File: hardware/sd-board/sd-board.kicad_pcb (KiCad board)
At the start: 2 copper layers, 22 x 71.1 mm, 9 parts, among them J1 TF-01A push-push, J2 FFC 6P 0.5mm, U1 74LVC1G04

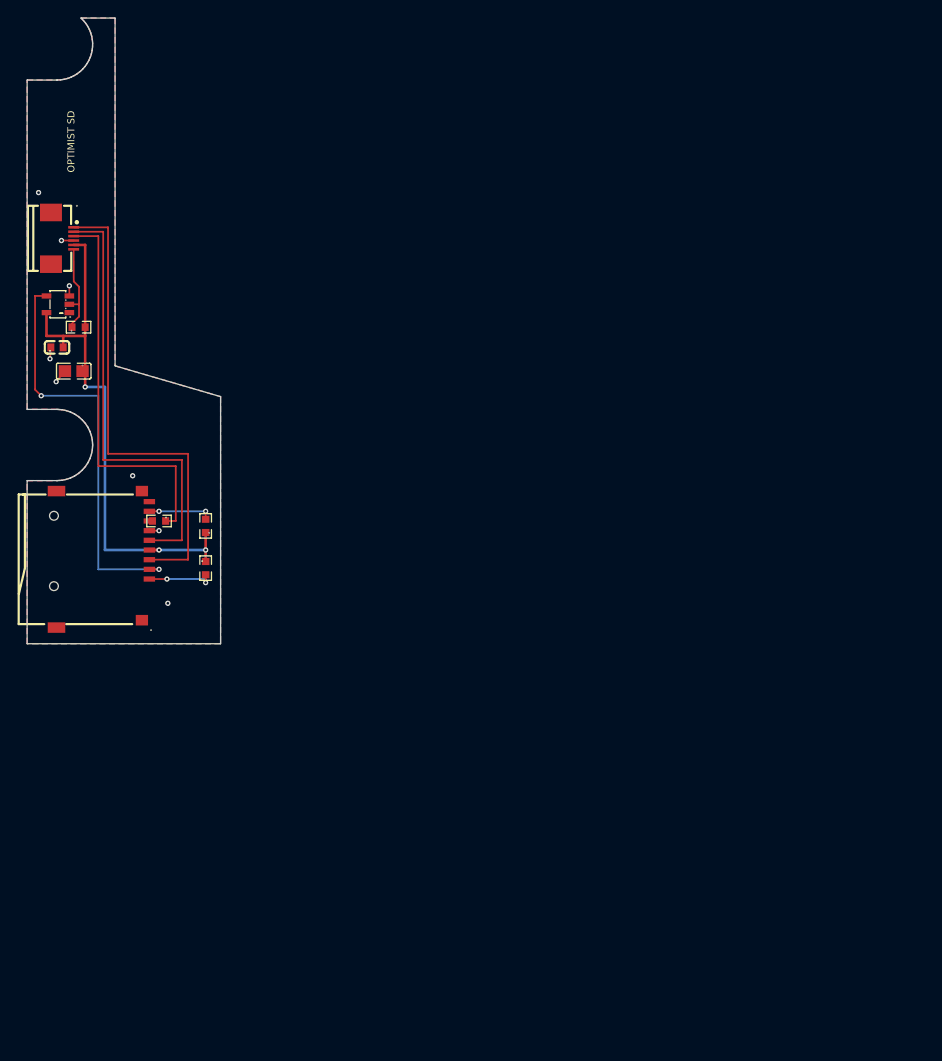
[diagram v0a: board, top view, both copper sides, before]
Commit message: feat(hardware): SD board v4, the user's plan: a 28.8 x 44.5 mm board right of the battery by its plug (the battery stays), the card through the bottom wall flush with the outside at 86 mm from the left wall, the cover's pole in a half-round seat, the FFC from the jacks' gap down to the top; FFC order 3V3 CS MOSI GND CLK MISO (the card's contacts' order, nothing crosses); all sizes measured (MEASUREMENTS.md); DRC 0, nets 0 differ
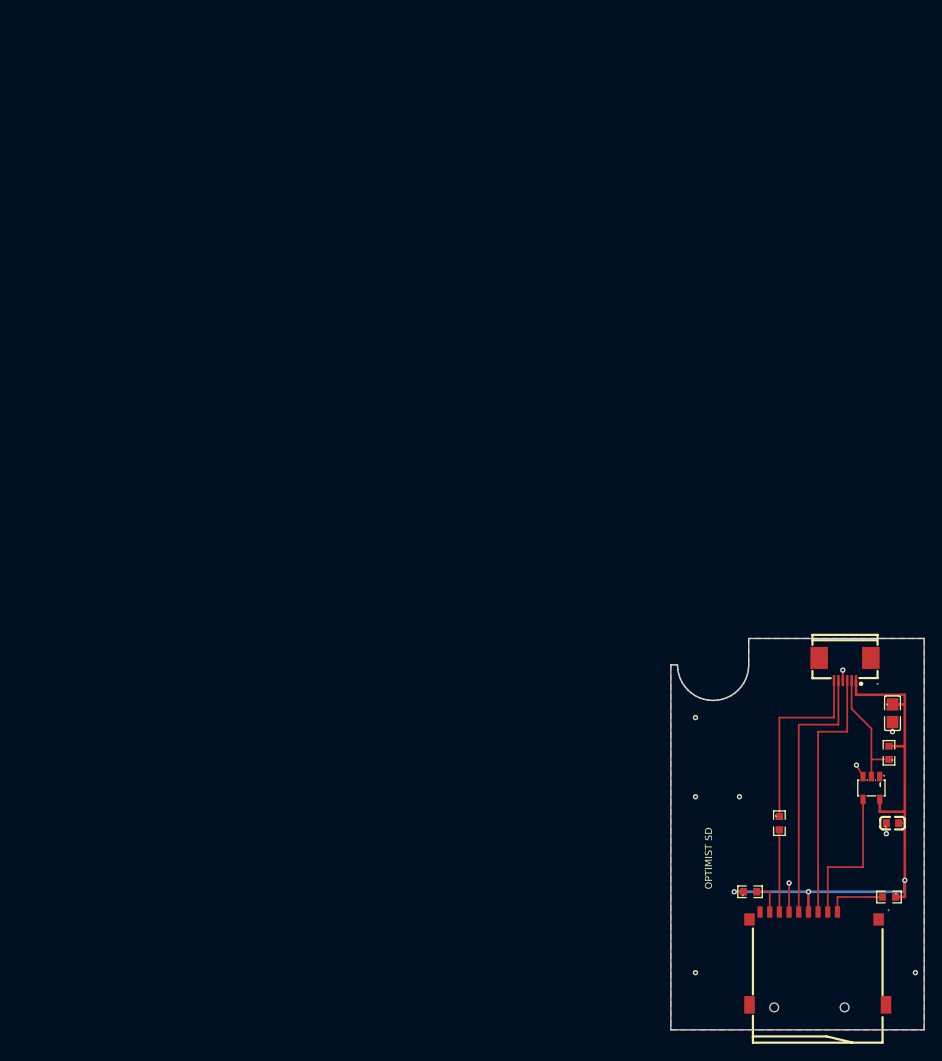
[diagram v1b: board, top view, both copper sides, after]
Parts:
- moved C2 109.3 mm to (198.4, 178.0)
- moved U1 107.6 mm to (196.0, 174.0), turned to 90 degrees
- moved R4 104.1 mm to (198.0, 170.0), turned to 90 degrees
- moved J2 101.6 mm to (193.0, 160.5), turned to 180 degrees
- moved C1 100.9 mm to (198.4, 165.5), turned to -90 degrees
- moved J1 93.1 mm to (189.9, 193.4), turned to 0 degrees
- moved R2 86.2 mm to (198.0, 186.4), turned to 180 degrees
- moved R1 78.5 mm to (185.5, 178.0), turned to -90 degrees
- moved R3 74.6 mm to (182.2, 185.8), turned to 0 degrees
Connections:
- J2 pad 1: MOSI -> 3V3
- J2 pad 2: CLK -> LCD_CS
- J2 pad 3: MISO -> MOSI
- J2 pad 5: 3V3 -> CLK
- J2 pad 6: LCD_CS -> MISO
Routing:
- net CARD_CS: track 47.2 -> 16.8 mm, vias 2 -> 0
- net MOSI: track 55.2 -> 29.6 mm
- net MISO: track 45.1 -> 21.7 mm
- net CLK: track 51.1 -> 30.8 mm
- net DAT0: track 0.35 -> 9.35 mm
- net DAT1: track 7.31 -> 3.79 mm, vias 2 -> 0
- net LCD_CS: track 10.5 -> 13.8 mm
- net GND: track 6.51 -> 8.29 mm, vias 8 -> 10
- net 3V3: track 62.4 -> 63.4 mm
- net DAT2: track 7.71 -> 6.81 mm, vias 2 -> 0
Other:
- board size 22 x 71.1 mm -> 28.8 x 44.5 mm

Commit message: feat(hardware): the SD board's printed tray (make_tray.py, sd-tray.stl, solid): a 0.8 mm floor, grooved rails the board slides into (held up and down; the board narrowed to 26.4 mm for them), a collar round the cover's pole that stops it, posts toward the cover; low elsewhere so the battery's cable crosses over (the user); the board's seat sized for the collar
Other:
- board size 28.8 x 44.5 mm -> 26.4 x 44.5 mm

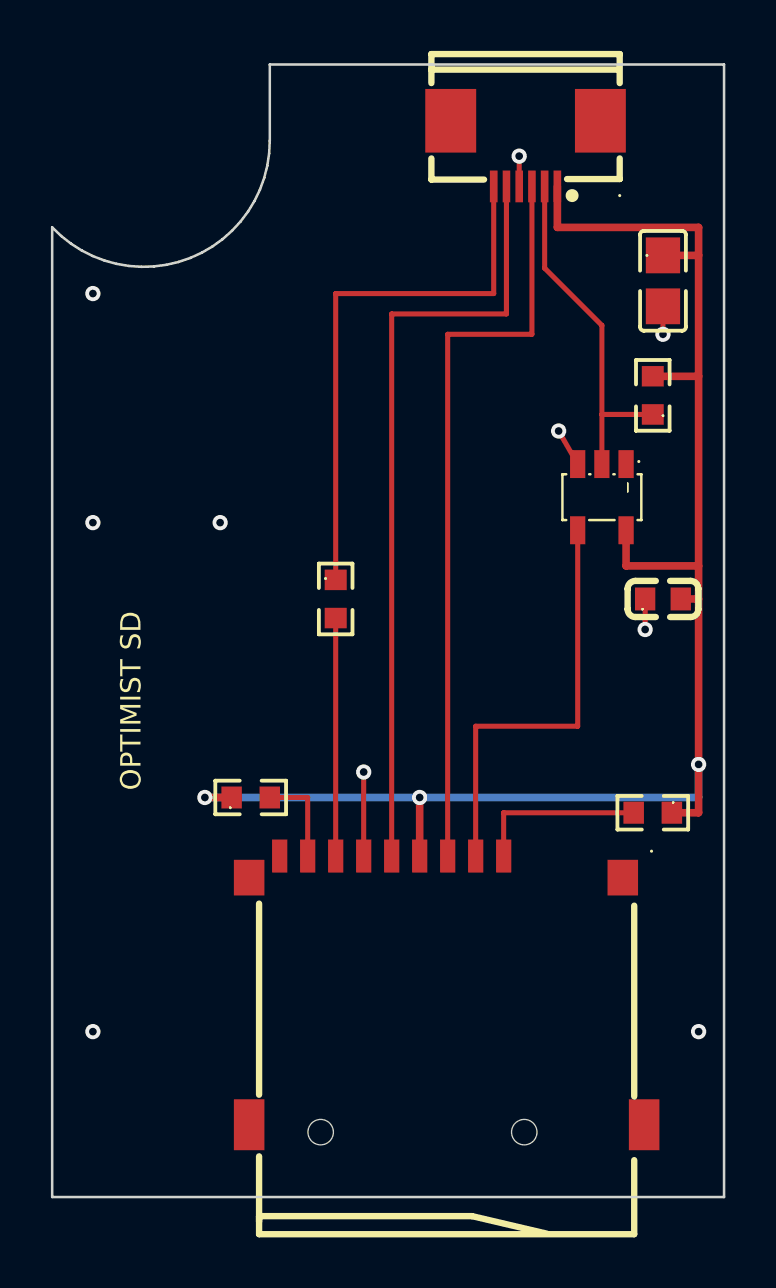
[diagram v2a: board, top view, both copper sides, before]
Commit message: feat(hardware): the SD board cut at the card socket's right edge (the user): 24.4 mm wide (74.4 to 98.8), U1 and its parts packed in the column right of the lines, the 3V3 rail at 97.8; the tray's right rail follows (to 100 mm, the plug at 102.6); DRC 0, nets 0 differ
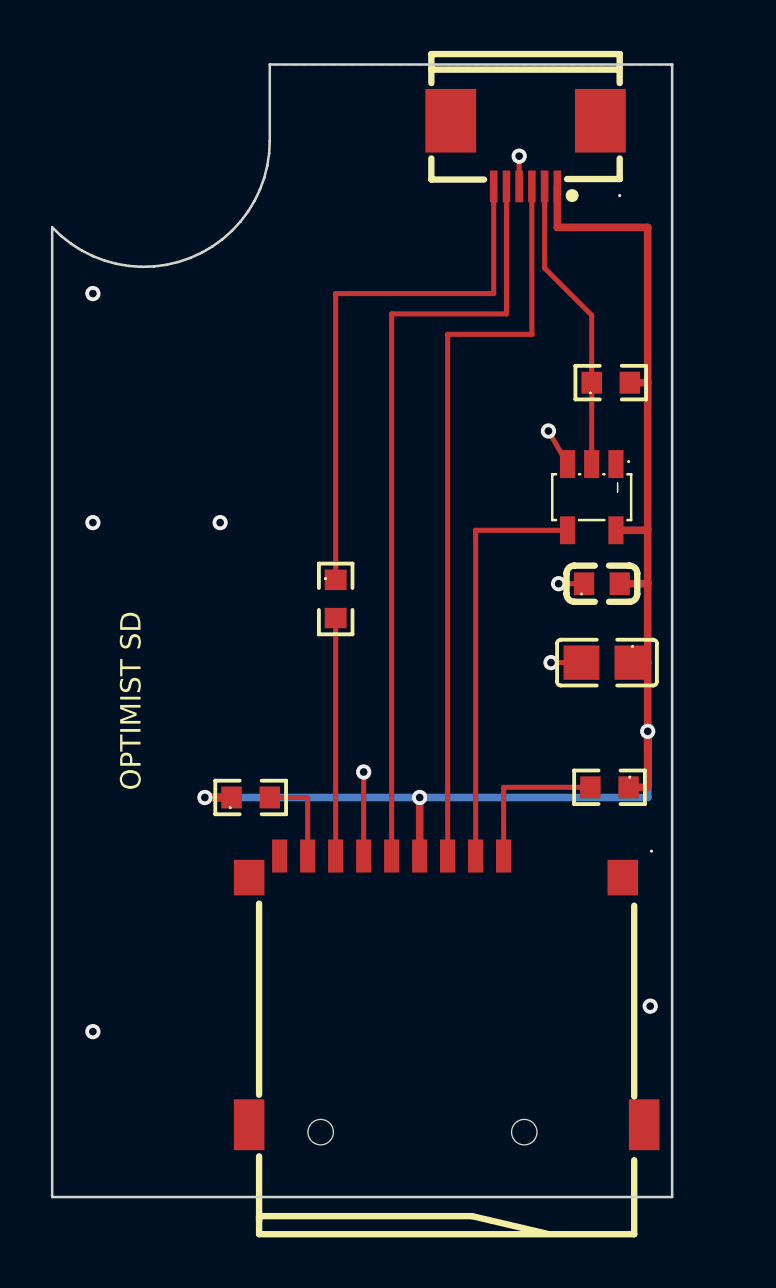
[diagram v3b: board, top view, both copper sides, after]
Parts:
- moved C1 15.2 mm to (196.2, 180.5), turned to 180 degrees
- moved C2 2.47 mm to (196.0, 177.4)
- moved R2 1.97 mm to (196.3, 185.4)
- moved R4 1.72 mm to (196.3, 169.5), turned to 0 degrees
- moved U1 0.40 mm to (195.6, 174.0)
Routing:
- net 3V3: track 63.4 -> 54.9 mm
- net LCD_CS: track 13.8 -> 11.7 mm
- net DAT2: track 6.81 -> 6.11 mm
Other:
- board size 26.4 x 44.5 mm -> 24.4 x 44.5 mm

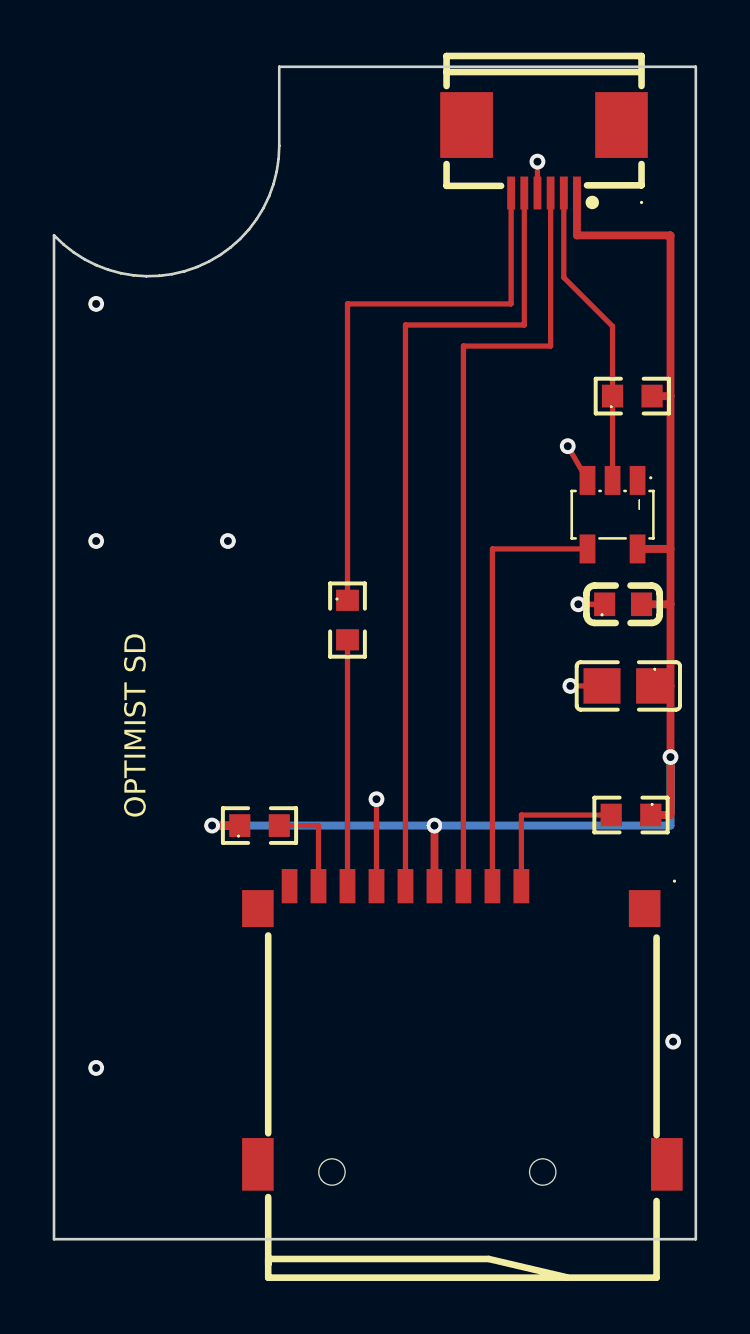
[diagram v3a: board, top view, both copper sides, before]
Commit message: feat(hardware): the card 2 mm left (84 mm from the left wall's inside, the user), the board 22.4 mm wide (to 96.8), the FFC socket at 91 (the jacks' gap at 90); the tray's posts leave the battery's cable a 24 to 40 mm gap (the user: bigger); DRC 0, nets 0 differ
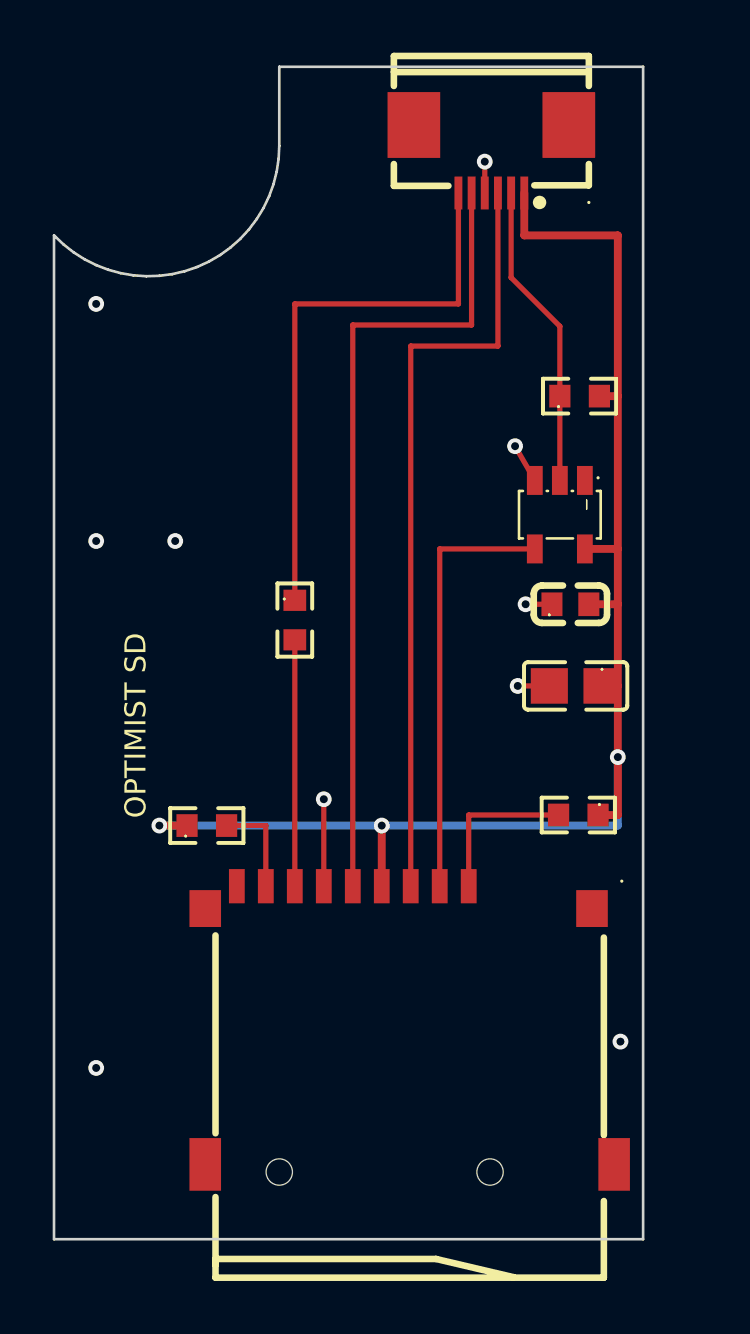
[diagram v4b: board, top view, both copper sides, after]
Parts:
- moved C1 2.00 mm to (194.2, 180.5)
- moved C2 2.00 mm to (194.0, 177.4)
- moved J1 2.00 mm to (187.9, 193.4)
- moved J2 2.00 mm to (191.0, 160.5)
- moved R1 2.00 mm to (183.5, 178.0)
- moved R2 2.00 mm to (194.3, 185.4)
- moved R3 2.00 mm to (180.2, 185.8)
- moved R4 2.00 mm to (194.3, 169.5)
- moved U1 2.00 mm to (193.6, 174.0)
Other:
- board size 24.4 x 44.5 mm -> 22.4 x 44.5 mm

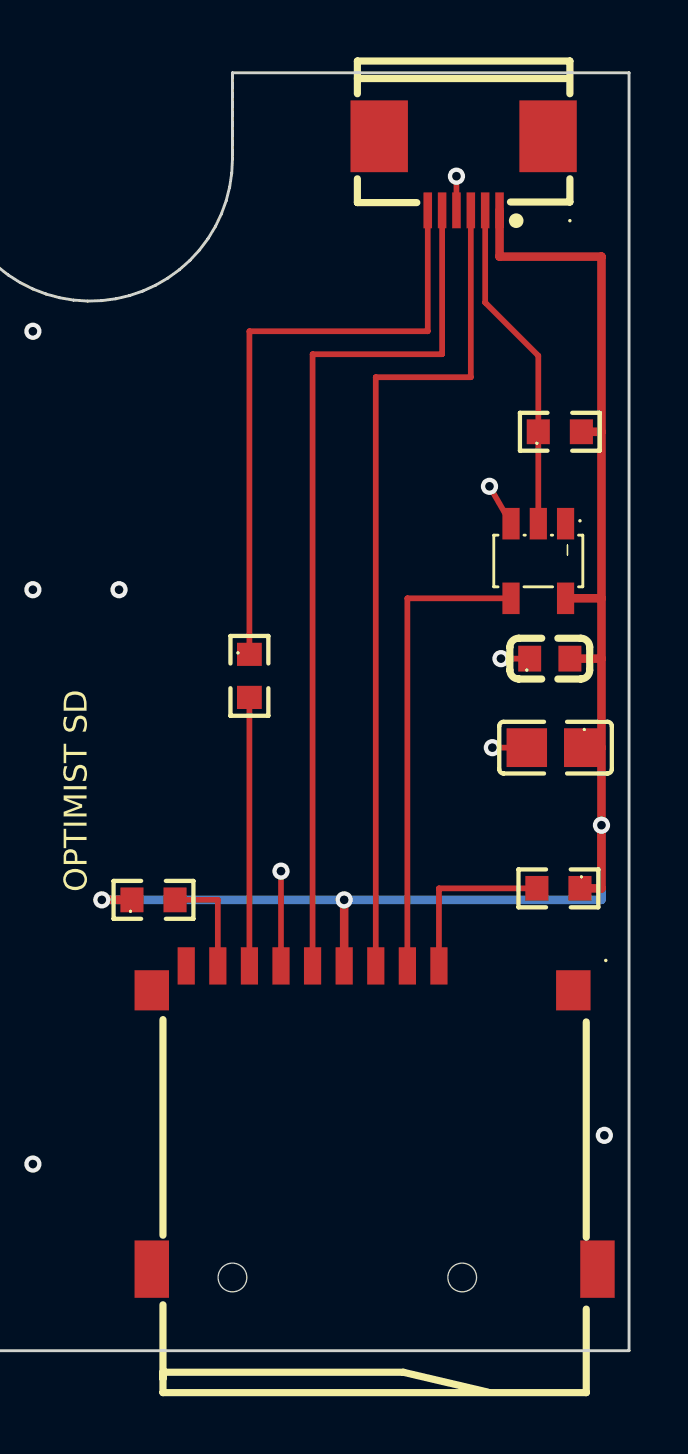
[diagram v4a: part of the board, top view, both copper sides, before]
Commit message: feat(hardware): the FFC socket 5 mm lower (34.5 mm up) so the ribbon comes down over the 4 mm speaker plug, and the board's top at the pole's centre (40 mm), 4 mm clear of the speaker plug (the user); the tray's top-right post gone; DRC 0, nets 0 differ
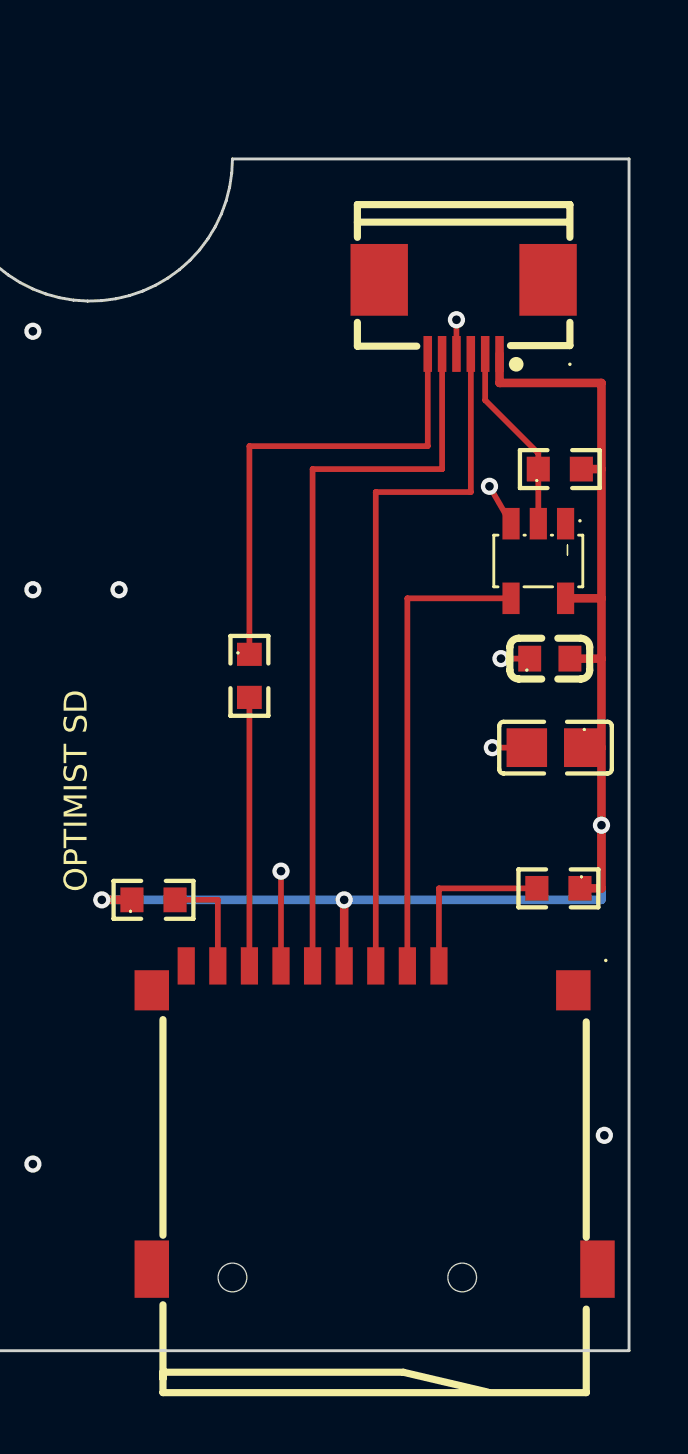
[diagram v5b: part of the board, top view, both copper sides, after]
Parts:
- moved J2 5.00 mm to (191.0, 165.5)
- moved R4 1.30 mm to (194.3, 170.8)
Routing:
- net MOSI: track 29.6 -> 24.6 mm
- net MISO: track 21.7 -> 16.7 mm
- net CLK: track 30.8 -> 25.8 mm
- net 3V3: track 54.9 -> 49.9 mm
- net LCD_CS: track 11.7 -> 6.68 mm
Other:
- board size 22.4 x 44.5 mm -> 22.4 x 41.5 mm
